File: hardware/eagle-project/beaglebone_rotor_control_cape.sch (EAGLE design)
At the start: 52 parts, among them IC1 TLC2264CDU, IC2 MCP4901, IC6 TLC2264CDU, Q1 SQ2348ES-T1-GE3, Q2 SQ2348ES-T1-GE3, Q3 SQ2348ES-T1-GE3, Q4 SQ2348ES-T1-GE3, Q5 SQ2348ES-T1-GE3, Q6 SQ2348ES-T1-GE3, U1 TMH0512S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

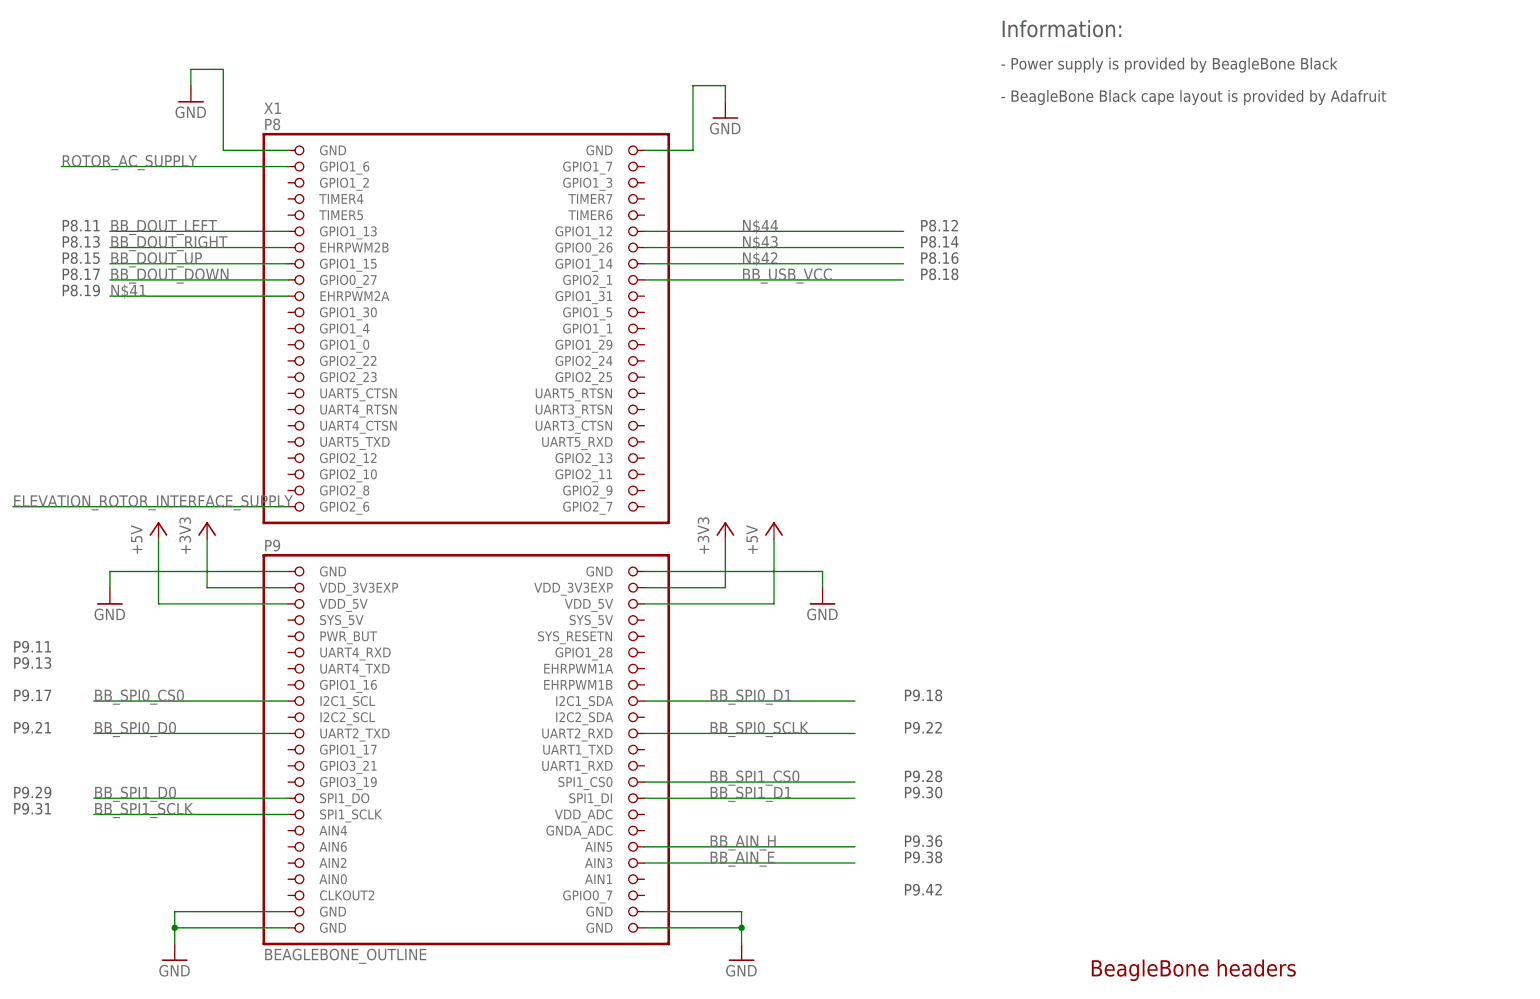
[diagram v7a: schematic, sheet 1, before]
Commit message: Improved Eagle layout, more free space on board for future components
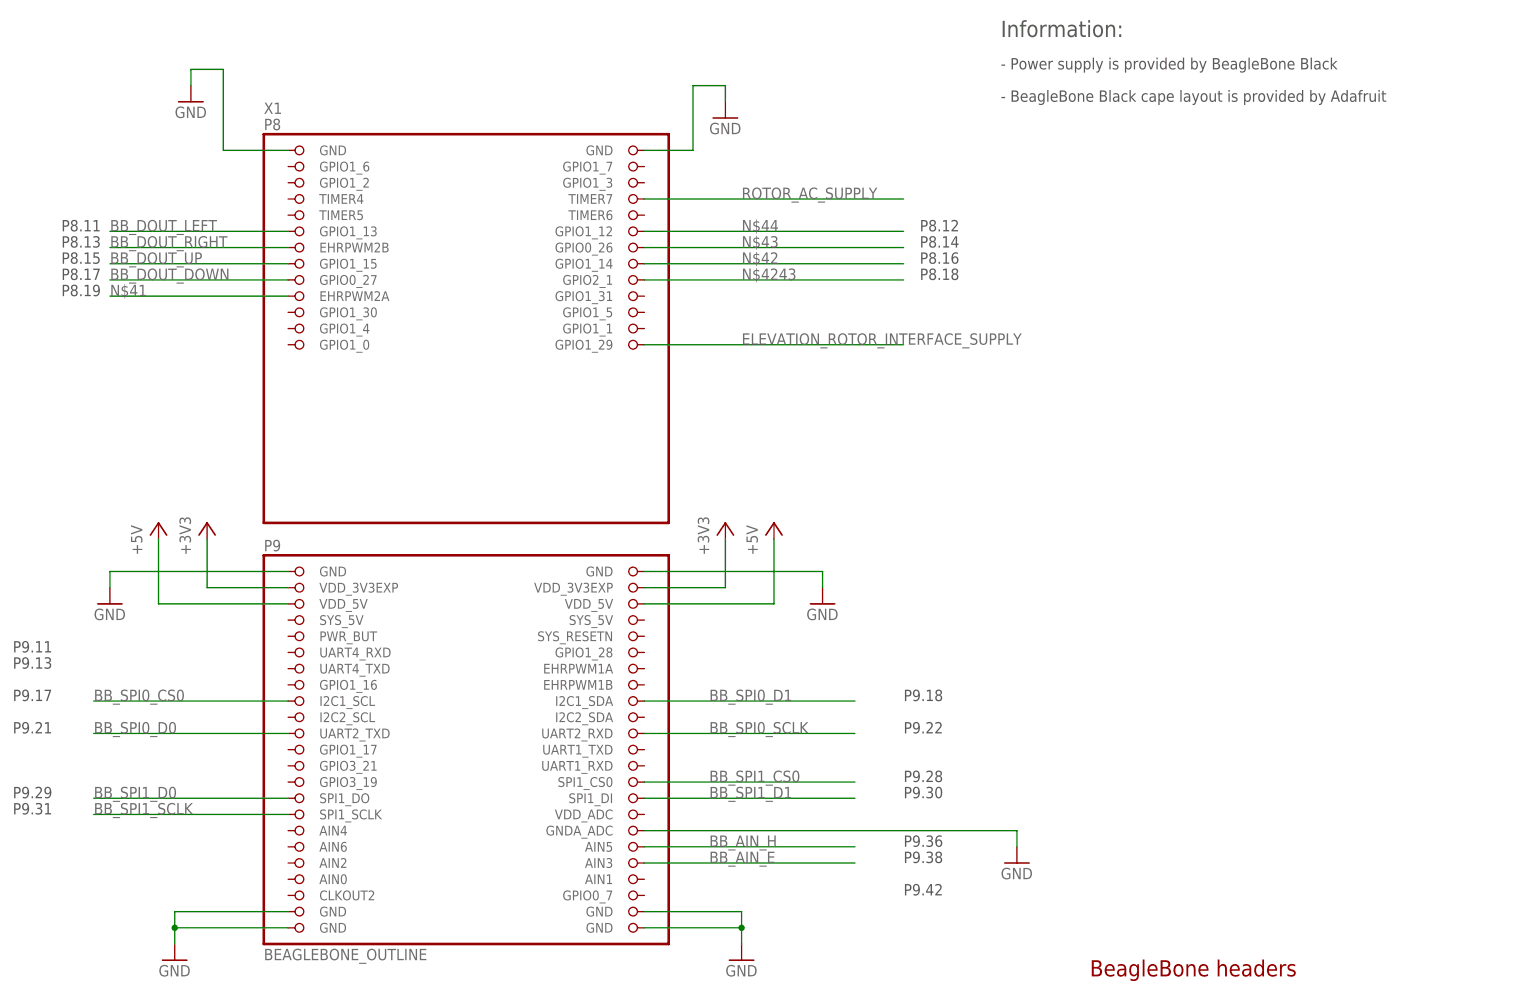
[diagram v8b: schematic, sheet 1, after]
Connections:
- net BB_USB_VCC renamed N$4243
- net +12V: now also X4.6
- net ELEVATION_ROTOR_INTERFACE_SUPPLY: now also X1.GPIO1_29; no longer X1.GPIO2_6
- net GND: now also X1.GNDA_ADC, X4.9; no longer X4.6
- net ROTOR_AC_SUPPLY: now also X1.TIMER7; no longer X1.GPIO1_6
- net ROT_E_DOWN: now also X4.7
- net ROT_E_UP: now also X4.8
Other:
- note removed: "wie open collector kurzschlussfest machen"
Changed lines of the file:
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@@
 <part name="C3" library="rcl" deviceset="C-EU" device="C0603" value="100n"/>
 <part name="GND12" library="supply1" deviceset="GND" device=""/>
+<part name="GND15" library="supply1" deviceset="GND" device=""/>
 </parts>
 <sheets>
@@
 <instance part="P+5" gate="1" x="33.02" y="91.44"/>
 <instance part="+3V2" gate="G$1" x="121.92" y="91.44"/>
+<instance part="GND15" gate="1" x="167.64" y="38.1"/>
 </instances>
 <busses>
@@
 <wire x1="121.92" y1="160.02" x2="121.92" y2="157.48" width="0.1524" layer="91"/>
 </segment>
+<segment>
+<pinref part="X1" gate="G$1" pin="GNDA_ADC"/>
+<wire x1="109.22" y1="43.18" x2="167.64" y2="43.18" width="0.1524" layer="91"/>
+<pinref part="GND15" gate="1" pin="GND"/>
+<wire x1="167.64" y1="43.18" x2="167.64" y2="40.64" width="0.1524" layer="91"/>
+</segment>
 </net>
 <net name="+3V3" class="0">
@@
 </segment>
 </net>
-<net name="BB_USB_VCC" class="0">
+<net name="N$4243" class="0">
 <segment>
 <pinref part="X1" gate="G$1" pin="GPIO2_1"/>
@@
 <net name="ELEVATION_ROTOR_INTERFACE_SUPPLY" class="0">
 <segment>
-<pinref part="X1" gate="G$1" pin="GPIO2_6"/>
-<wire x1="53.34" y1="93.98" x2="10.16" y2="93.98" width="0.1524" layer="91"/>
-<label x="10.16" y="93.98" size="1.778" layer="95"/>
+<pinref part="X1" gate="G$1" pin="GPIO1_29"/>
+<wire x1="109.22" y1="119.38" x2="149.86" y2="119.38" width="0.1524" layer="91"/>
+<label x="124.46" y="119.38" size="1.778" layer="95"/>
 </segment>
 </net>
 <net name="ROTOR_AC_SUPPLY" class="0">
 <segment>
-<pinref part="X1" gate="G$1" pin="GPIO1_6"/>
-<wire x1="53.34" y1="147.32" x2="17.78" y2="147.32" width="0.1524" layer="91"/>
-<label x="17.78" y="147.32" size="1.778" layer="95"/>
+<pinref part="X1" gate="G$1" pin="TIMER7"/>
+<wire x1="109.22" y1="142.24" x2="149.86" y2="142.24" width="0.1524" layer="91"/>
+<label x="124.46" y="142.24" size="1.778" layer="95"/>
 </segment>
 </net>
@@
 &gt;&gt; nachmessen!</text>
 <text x="76.2" y="116.84" size="1.778" layer="97">Vcc=5V</text>
-<text x="218.44" y="127" size="1.778" layer="97">wie open collector
-kurzschlussfest machen</text>
 <text x="40.64" y="38.1" size="1.778" layer="97" rot="R180">tie to GND for
 immediate
@@
 <text x="179.07" y="20.32" size="2.54" layer="94">Create ERC5-A control</text>
 <text x="15.24" y="144.78" size="2.54" layer="97">Position Input (analog, 0V - 5V)</text>
-<text x="106.68" y="127" size="1.778" layer="97" rot="R90">lieber Uz=4.7V?, aber
-Signal geht bis 5V (???)
-&gt;&gt; nachmessen!</text>
 <text x="76.2" y="119.38" size="1.778" layer="97">Vcc=5V</text>
 <text x="12.7" y="157.48" size="5.08" layer="97">Create ERC-5AP</text>
 <text x="144.78" y="154.94" size="2.54" layer="97">UP (open collector)</text>
 <text x="144.78" y="83.82" size="2.54" layer="97">DOWN (open collector)</text>
-<text x="218.44" y="121.92" size="1.778" layer="97">wie open collector
-kurzschlussfest machen</text>
 </plain>
 <instances>
@@
 <plain>
 <text x="179.07" y="20.32" size="2.54" layer="94">Rotor connectors</text>
-<text x="91.44" y="116.84" size="2.54" layer="97">Connector</text>
+<text x="86.36" y="121.92" size="2.54" layer="97">Connector</text>
 </plain>
 <instances>
 <instance part="FRAME7" gate="G$1" x="0" y="0"/>
-<instance part="GND34" gate="1" x="139.7" y="93.98"/>
+<instance part="GND34" gate="1" x="165.1" y="109.22" rot="R90"/>
 <instance part="X4" gate="G$1" x="127" y="106.68" rot="R180"/>
-<instance part="P+14" gate="1" x="142.24" y="129.54"/>
+<instance part="P+14" gate="1" x="167.64" y="101.6" rot="R270"/>
 </instances>
 <busses>
@@
 <net name="GND" class="0">
 <segment>
-<wire x1="134.62" y1="101.6" x2="139.7" y2="101.6" width="0.1524" layer="91"/>
 <pinref part="GND34" gate="1" pin="GND"/>
-<wire x1="139.7" y1="101.6" x2="139.7" y2="96.52" width="0.1524" layer="91"/>
-<pinref part="X4" gate="G$1" pin="6"/>
+<wire x1="134.62" y1="109.22" x2="162.56" y2="109.22" width="0.1524" layer="91"/>
+<pinref part="X4" gate="G$1" pin="9"/>
 </segment>
 </net>
@@
 </segment>
 </net>
-<net name="ROT_E_SPEED" class="0">
-<segment>
-<wire x1="139.7" y1="109.22" x2="167.64" y2="109.22" width="0.1524" layer="91"/>
-<label x="139.7" y="109.22" size="1.778" layer="95"/>
-</segment>
-</net>
 <net name="ROT_E_POSITION" class="0">
 <segment>
@@
 <net name="ROT_E_DOWN" class="0">
 <segment>
-<wire x1="167.64" y1="104.14" x2="139.7" y2="104.14" width="0.1524" layer="91"/>
-<label x="139.7" y="104.14" size="1.778" layer="95"/>
+<wire x1="162.56" y1="104.14" x2="134.62" y2="104.14" width="0.1524" layer="91"/>
+<label x="137.16" y="104.14" size="1.778" layer="95"/>
+<pinref part="X4" gate="G$1" pin="7"/>
 </segment>
 </net>
 <net name="ROT_E_UP" class="0">
 <segment>
-<wire x1="139.7" y1="106.68" x2="167.64" y2="106.68" width="0.1524" layer="91"/>
-<label x="139.7" y="106.68" size="1.778" layer="95"/>
+<wire x1="134.62" y1="106.68" x2="162.56" y2="106.68" width="0.1524" layer="91"/>
+<label x="137.16" y="106.68" size="1.778" layer="95"/>
+<pinref part="X4" gate="G$1" pin="8"/>
 </segment>
 </net>
@@
 <segment>
 <pinref part="P+14" gate="1" pin="+12V"/>
-<wire x1="142.24" y1="127" x2="142.24" y2="116.84" width="0.1524" layer="91"/>
+<wire x1="165.1" y1="101.6" x2="134.62" y2="101.6" width="0.1524" layer="91"/>
+<pinref part="X4" gate="G$1" pin="6"/>
 </segment>
 </net>
@@
 <plain>
 <text x="179.07" y="20.32" size="2.54" layer="94">Elevation rotor interface supply</text>
-<text x="43.18" y="134.62" size="2.54" layer="97">There is a relay built into the Create ERC-5A which
+<text x="35.56" y="124.46" size="2.54" layer="97">There is a relay built into the Create ERC-5A which
 toggles control between this board and the manual
 switches. It is powerd by this 12V supply.
